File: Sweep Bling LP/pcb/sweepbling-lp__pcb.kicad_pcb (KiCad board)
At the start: 2 copper layers, 216.9 x 86.9 mm, 56 parts, among them SW1 SW_Push, SW10 SW_Push, SW10_r1 SW_Push, SW11 SW_Push, SW11_r1 SW_Push, SW12 SW_Push, SW12_r1 SW_Push, SW13 SW_Push, SW13_r1 SW_Push, SW14 SW_Push, SW14_r1 SW_Push, SW15 SW_Push, SW15_r1 SW_Push, SW16 SW_Push, SW16_r1 SW_Push, SW17 SW_Push, SW17_r1 SW_Push, SW1_r1 SW_Push, SW2 SW_Push, SW2_r1 SW_Push, SW3 SW_Push, SW3_r1 SW_Push, SW4 SW_Push, SW4_r1 SW_Push, SW5 SW_Push, SW5_r1 SW_Push, SW6 SW_Push, SW6_r1 SW_Push, SW7 SW_Push, SW7_r1 SW_Push, SW8 SW_Push, SW8_r1 SW_Push, SW9 SW_Push, SW9_r1 SW_Push, U1 ProMicro-kbd, U2 ProMicro-kbd

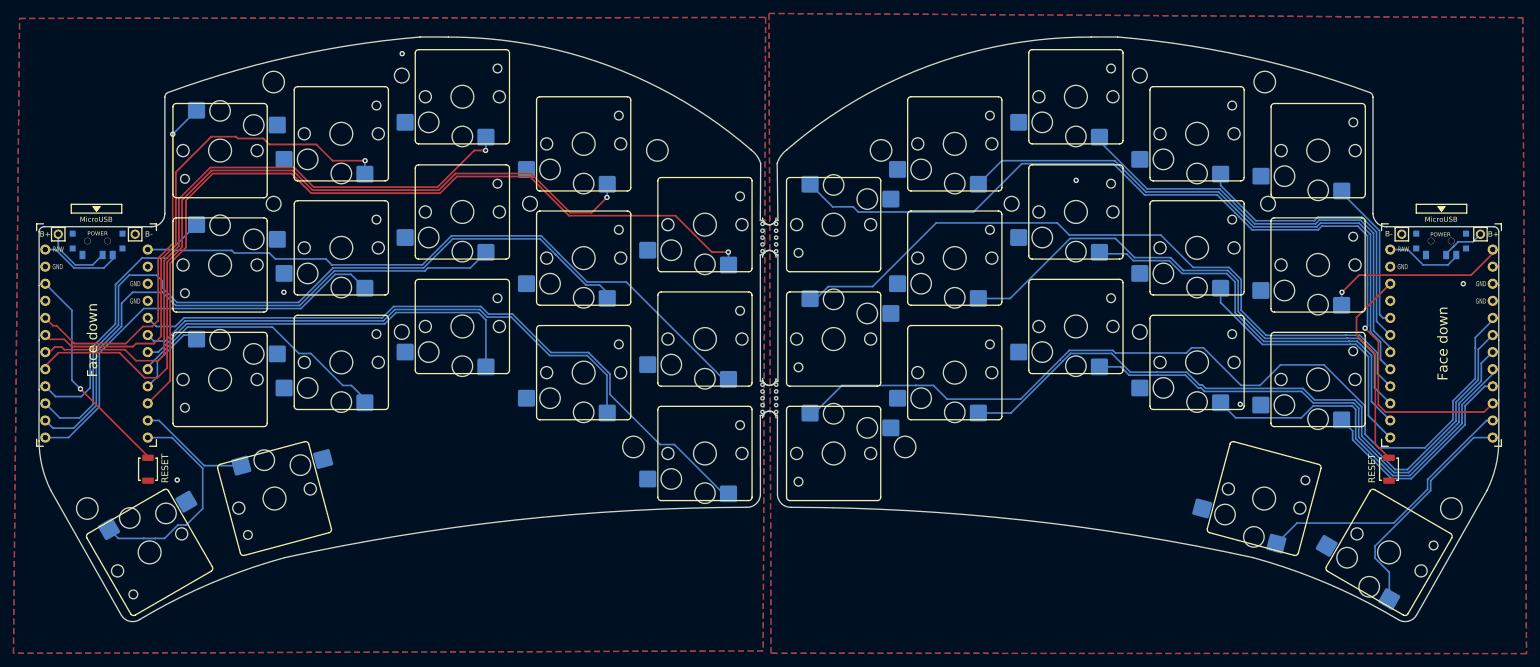
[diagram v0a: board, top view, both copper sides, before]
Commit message: replace key markings
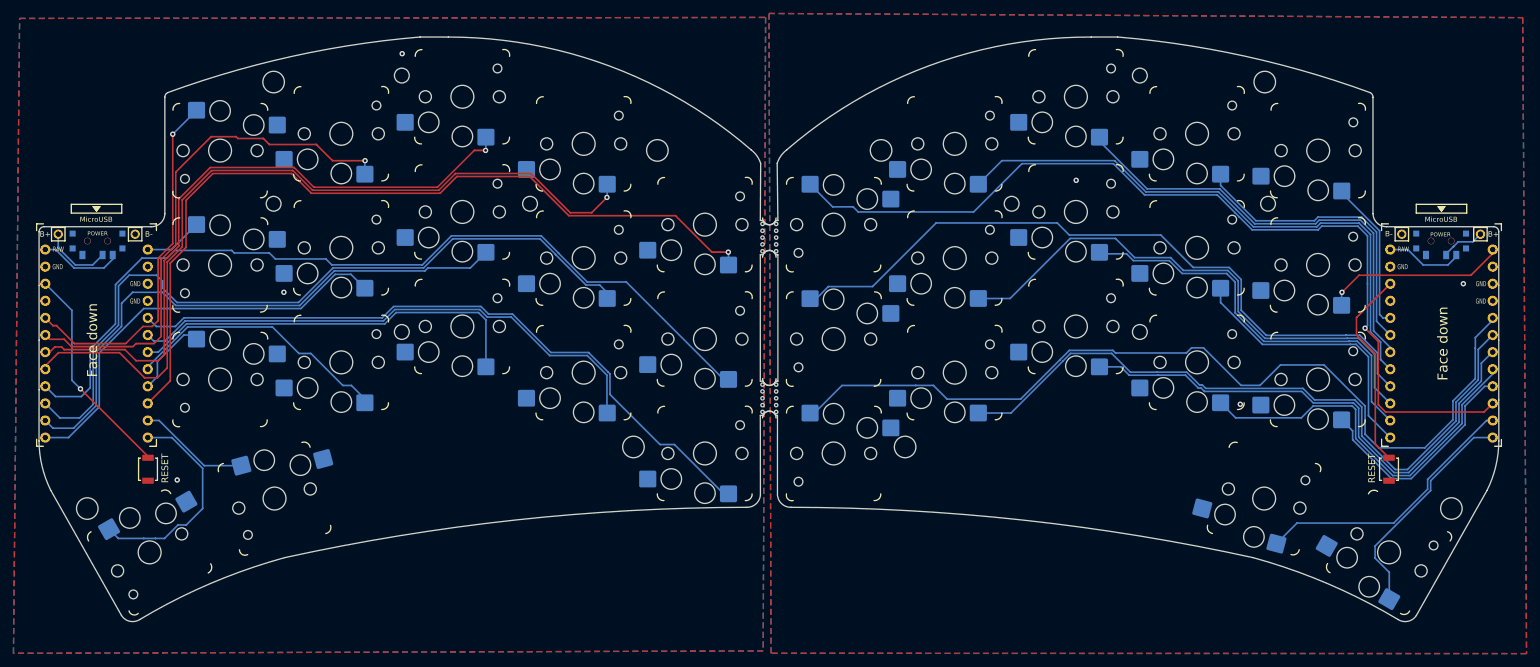
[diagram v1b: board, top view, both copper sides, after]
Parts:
- SW1, SW10, SW10_r1, SW11, SW11_r1, SW12, SW12_r1, SW13, SW13_r1, SW14, SW14_r1, SW15, SW15_r1, SW16, SW16_r1, SW17, SW17_r1, SW1_r1, SW2, SW2_r1, SW3, SW3_r1, SW4, SW4_r1, SW5, SW5_r1, SW6, SW6_r1, SW7, SW7_r1, SW8, SW8_r1, SW9, SW9_r1: footprint * duckyb-collection:SW_Hotswap_Kailh_Choc_V1_tweaked -> scda:SW_Hotswap_Kailh_Choc_V1_tweaked_only_corners

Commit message: move reset buttons
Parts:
- moved RSW2 12.6 mm to (25.4, 85.7)
- moved RSW1 12.6 mm to (234.9, 85.7)
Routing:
- net reset: track 29.9 -> 42.5 mm
- net reset_r: track 32.6 -> 29.1 mm
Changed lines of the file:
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@@
   )
   (footprint "kbd:SW_SPST_B3U-1000P" (layer "F.Cu")
-    (at 222.377 85.725 90)
+    (at 234.95 85.725 90)
     (descr "Ultra-small-sized Tactile Switch with High Contact Reliability, Top-actuated Model, without Ground Terminal, without Boss")
     (tags "Tactile Switch")
@@
     )
     (fp_text value "SW_Push" (at 0 -2.55 90) (layer "F.Fab")
-      (effects (font (size 1 1) (thickness 0.15)))
-    )
-    (fp_text user "RESET" (at 0.127 -2.540504 90) (layer "F.SilkS")
       (effects (font (size 1 1) (thickness 0.15)))
     )
@@
   )
   (footprint "kbd:SW_SPST_B3U-1000P" (layer "F.Cu")
-    (at 37.973 85.725 90)
+    (at 25.4 85.725 90)
     (descr "Ultra-small-sized Tactile Switch with High Contact Reliability, Top-actuated Model, without Ground Terminal, without Boss")
     (tags "Tactile Switch")
@@
     )
     (fp_text value "SW_Push" (at 0 -2.55 90) (layer "F.Fab")
-      (effects (font (size 1 1) (thickness 0.15)))
-    )
-    (fp_text user "RESET" (at 0.127 2.535537 90) (layer "F.SilkS")
       (effects (font (size 1 1) (thickness 0.15)))
     )
@@
   (via (at 175.895 42.799) (size 0.8) (drill 0.4) (layers "F.Cu" "B.Cu") (free) (net 1))
   (via (at 233.426 58.166) (size 0.8) (drill 0.4) (layers "F.Cu" "B.Cu") (free) (net 1))
+  (segment (start 222.377 84.025) (end 234.95 84.025) (width 0.25) (layer "F.Cu") (net 4))
   (segment (start 217.551 65.786) (end 220.345 68.58) (width 0.25) (layer "F.Cu") (net 4))
   (segment (start 217.551 63.1844) (end 217.551 65.786) (width 0.25) (layer "F.Cu") (net 4))
@@
   (segment (start 24.638 52.832) (end 27.178 55.372) (width 0.25) (layer "B.Cu") (net 23))
   (segment (start 27.178 55.372) (end 29.749 55.372) (width 0.25) (layer "B.Cu") (net 23))
-  (segment (start 37.973 83.693) (end 37.973 84.152) (width 0.25) (layer "F.Cu") (net 25))
-  (segment (start 37.973 84.025) (end 37.973 83.82) (width 0.25) (layer "F.Cu") (net 25))
-  (segment (start 37.973 83.82) (end 27.94 73.787) (width 0.25) (layer "F.Cu") (net 25))
+  (segment (start 25.4 83.82) (end 25.4 84.025) (width 0.25) (layer "F.Cu") (net 25))
+  (segment (start 27.94 81.28) (end 25.4 83.82) (width 0.25) (layer "F.Cu") (net 25))
+  (segment (start 27.94 81.28) (end 27.94 73.787) (width 0.25) (layer "F.Cu") (net 25))
   (via (at 27.94 73.787) (size 0.8) (drill 0.4) (layers "F.Cu" "B.Cu") (net 25))
   (segment (start 26.67 62.1186) (end 22.7174 58.166) (width 0.25) (layer "B.Cu") (net 25))

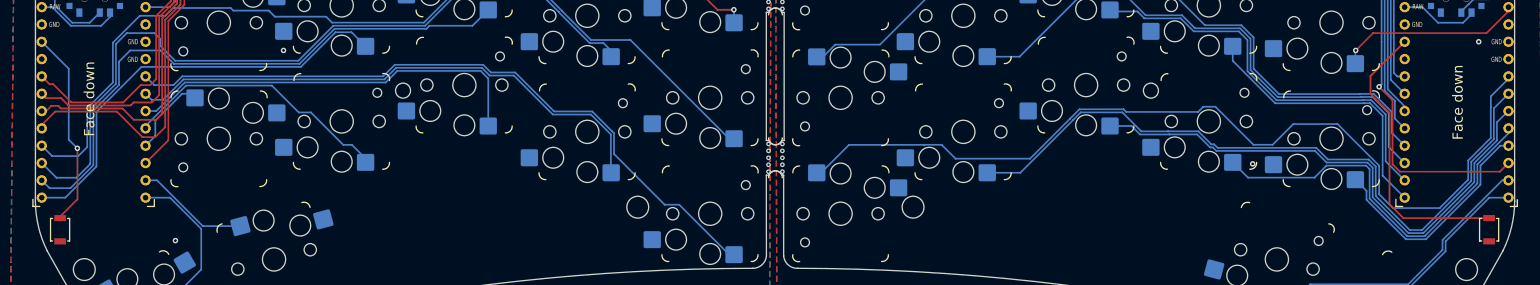
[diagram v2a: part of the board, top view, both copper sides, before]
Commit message: drop reset pads
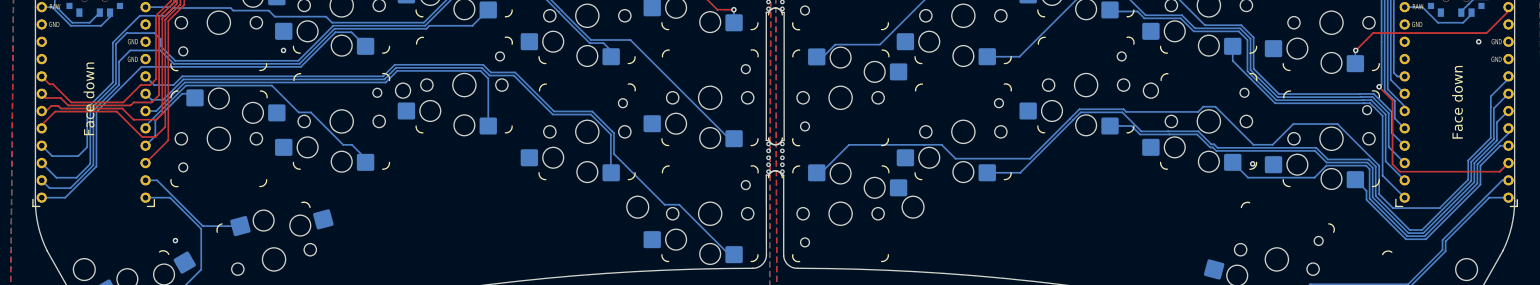
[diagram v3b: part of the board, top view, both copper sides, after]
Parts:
- removed RSW1, RSW2: SW_Push, kbd:SW_SPST_B3U-1000P
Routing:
- net reset: track 42.5 -> 0.00 mm
- net reset_r: track 29.1 -> 0.00 mm, vias 1 -> 0
